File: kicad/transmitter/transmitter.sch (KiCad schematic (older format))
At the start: 30 parts, among them J1 Conn_01x02, J2 Conn_01x04, J3 AudioJack3, J4 AudioJack3, SW1 SW_SPST, SW2 SW_SPST, U1 ATmega328P-PU, U2 NRF24L01_Breakout, U3 MH-M18, U4 MSGEQ7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

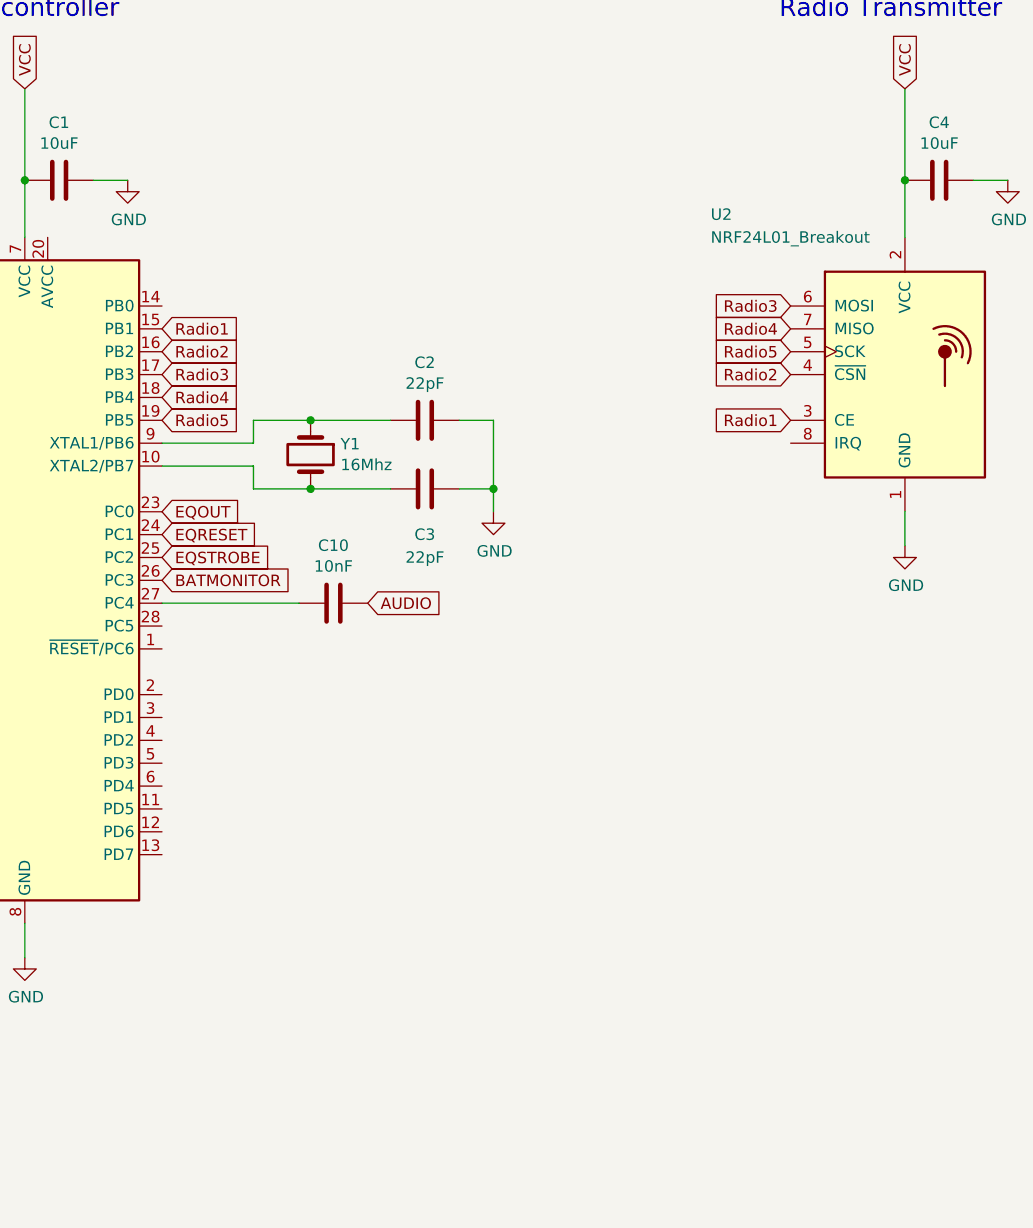
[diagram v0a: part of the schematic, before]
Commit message: Button, LEDs, ICSP header
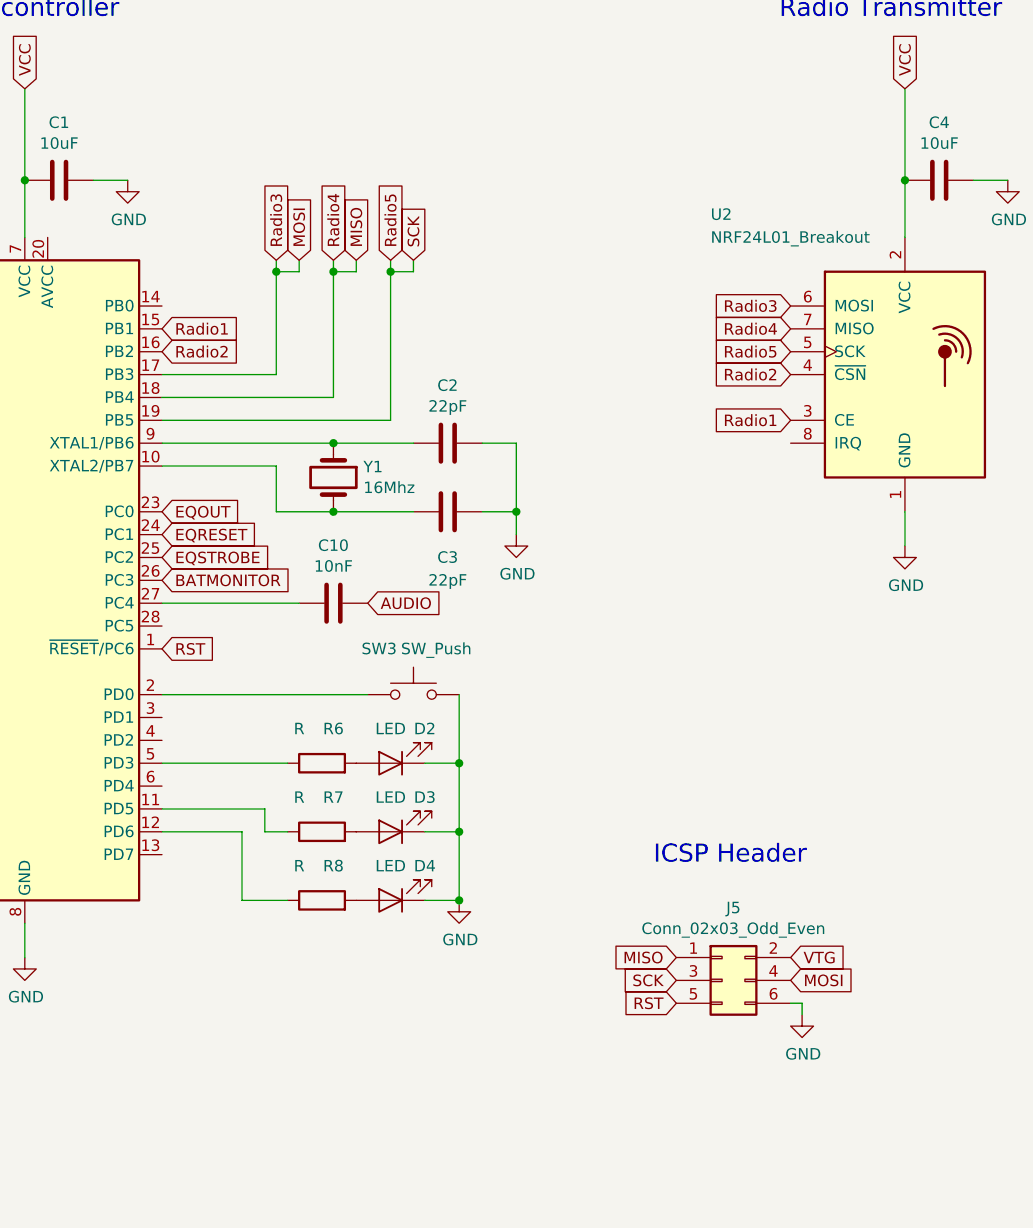
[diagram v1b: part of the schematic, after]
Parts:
- added D2, D3, D4: LED, LED_THT:LED_D3.0mm, symbol Device:LED
- added J5: Conn_02x03_Odd_Even, Connector_PinHeader_2.54mm:PinHeader_2x03_P2.54mm_Vertical, symbol Connector_Generic:Conn_02x03_Odd_Even
- added R6, R7, R8: R, Resistor_SMD:R_0603_1608Metric_Pad1.05x0.95mm_HandSolder, symbol Device:R
- added SW3: SW_Push, Connector_PinHeader_2.54mm:PinHeader_1x02_P2.54mm_Vertical, symbol Switch:SW_Push
- SW1, SW2: footprint Connector_Wire:SolderWirePad_1x02_P3.81mm_Drill1mm -> Connector_PinHeader_2.54mm:PinHeader_1x02_P2.54mm_Vertical
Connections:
- net GND: now also D2.1 (K), D3.1 (K), D4.1 (K), J5.6 (Pin_6), SW3.2
- net Radio5: now also J5.3 (Pin_3)
- net RST: now reaches U1.1 (~RESET~/PC6)
- net RST: now also J5.5 (Pin_5)
- net at U1.11 (PD5): now also R7.1
- net at U1.12 (PD6): now also R8.1
- net at U1.2 (PD0): now also SW3.1
- net at U1.5 (PD3): now also R6.1
- net Radio3 renamed MOSI
- net MOSI: now also J5.4 (Pin_4)
- net Radio4 renamed MISO
- net MISO: now also J5.1 (Pin_1)
- new net: D2.2 (A), R6.2
- new net: D3.2 (A), R7.2
- new net: D4.2 (A), R8.2
- new net VTG: J5.2 (Pin_2)
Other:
- note added: "ICSP Header"
- moved on the sheet: C2, C3, Y1

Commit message: Tidy-ups pre-order
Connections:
- no-connect marks 2 -> 9
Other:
- moved on the sheet: J5
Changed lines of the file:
@@
 L Connector_Generic:Conn_02x03_Odd_Even J5
 U 1 1 5E8614B4
-P 9250 5050
-F 0 "J5" H 9300 5367 50  0000 C CNN
-F 1 "Conn_02x03_Odd_Even" H 9300 5276 50  0000 C CNN
-F 2 "Connector_PinHeader_2.54mm:PinHeader_2x03_P2.54mm_Vertical" H 9250 5050 50  0001 C CNN
-F 3 "~" H 9250 5050 50  0001 C CNN
-	1    9250 5050
-	1    0    0    -1
-$EndComp
-Text GLabel 9050 4950 0    50   Input ~ 0
+P 9650 5350
+F 0 "J5" H 9700 5667 50  0000 C CNN
+F 1 "Conn_02x03_Odd_Even" H 9700 5576 50  0000 C CNN
+F 2 "Connector_PinHeader_2.54mm:PinHeader_2x03_P2.54mm_Vertical" H 9650 5350 50  0001 C CNN
+F 3 "~" H 9650 5350 50  0001 C CNN
+	1    9650 5350
+	1    0    0    -1
+$EndComp
+Text GLabel 9450 5250 0    50   Input ~ 0
 MISO
-Text GLabel 9550 4950 2    50   Input ~ 0
+Text GLabel 9950 5250 2    50   Input ~ 0
 VTG
-Text GLabel 9050 5050 0    50   Input ~ 0
+Text GLabel 9450 5350 0    50   Input ~ 0
 SCK
-Text GLabel 9550 5050 2    50   Input ~ 0
+Text GLabel 9950 5350 2    50   Input ~ 0
 MOSI
-Text GLabel 9050 5150 0    50   Input ~ 0
+Text GLabel 9450 5450 0    50   Input ~ 0
 RST
 $Comp
 L power:GND #PWR0118
 U 1 1 5E865C55
-P 9600 5200
-F 0 "#PWR0118" H 9600 4950 50  0001 C CNN
-F 1 "GND" H 9605 5027 50  0000 C CNN
-F 2 "" H 9600 5200 50  0001 C CNN
-F 3 "" H 9600 5200 50  0001 C CNN
-	1    9600 5200
-	1    0    0    -1
-$EndComp
-Wire Wire Line
-	9550 5150 9600 5150
-Wire Wire Line
-	9600 5150 9600 5200
-Text Notes 8950 4550 0    79   ~ 0
+P 10000 5500
+F 0 "#PWR0118" H 10000 5250 50  0001 C CNN
+F 1 "GND" H 10005 5327 50  0000 C CNN
+F 2 "" H 10000 5500 50  0001 C CNN
+F 3 "" H 10000 5500 50  0001 C CNN
+	1    10000 5500
+	1    0    0    -1
+$EndComp
+Wire Wire Line
+	9950 5450 10000 5450
+Wire Wire Line
+	10000 5450 10000 5500
+Text Notes 9350 4850 0    79   ~ 0
 ICSP Header
 Text GLabel 6800 3600 2    50   Input ~ 0
@@
 L power:GND #PWR0119
 U 1 1 5E43BBB8
-P 8100 4700
-F 0 "#PWR0119" H 8100 4450 50  0001 C CNN
-F 1 "GND" H 8105 4527 50  0000 C CNN
-F 2 "" H 8100 4700 50  0001 C CNN
-F 3 "" H 8100 4700 50  0001 C CNN
-	1    8100 4700
+P 8100 4950
+F 0 "#PWR0119" H 8100 4700 50  0001 C CNN
+F 1 "GND" H 8105 4777 50  0000 C CNN
+F 2 "" H 8100 4950 50  0001 C CNN
+F 3 "" H 8100 4950 50  0001 C CNN
+	1    8100 4950
 	1    0    0    -1
 $EndComp
@@
 Wire Wire Line
 	7950 4700 8100 4700
-Connection ~ 8100 4700
 Wire Wire Line
 	7950 4400 8100 4400
@@
 	8100 3800 8100 4100
 Connection ~ 8100 4100
+NoConn ~ 6800 3500
+NoConn ~ 6800 3900
+NoConn ~ 6800 4000
+NoConn ~ 6800 4200
+NoConn ~ 6800 4500
+NoConn ~ 6800 2100
+NoConn ~ 9550 2700
+Wire Wire Line
+	8100 4700 8100 4950
+Connection ~ 8100 4700
 $EndSCHEMATC

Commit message: Resistor and capacitor values
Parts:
- R3: value R -> 200k
- R4: value R -> 270k
- R5: value R -> 100k
- R6, R7, R8: value R -> 510
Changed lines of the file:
@@
 P 3800 6600
 F 0 "R3" V 3593 6600 50  0000 C CNN
-F 1 "R" V 3684 6600 50  0000 C CNN
+F 1 "200k" V 3684 6600 50  0000 C CNN
 F 2 "Resistor_SMD:R_0603_1608Metric_Pad1.05x0.95mm_HandSolder" V 3730 6600 50  0001 C CNN
 F 3 "~" H 3800 6600 50  0001 C CNN
@@
 P 3150 1550
 F 0 "R4" H 3080 1504 50  0000 R CNN
-F 1 "R" H 3080 1595 50  0000 R CNN
+F 1 "270k" H 3080 1595 50  0000 R CNN
 F 2 "Resistor_SMD:R_0603_1608Metric_Pad1.05x0.95mm_HandSolder" V 3080 1550 50  0001 C CNN
 F 3 "~" H 3150 1550 50  0001 C CNN
@@
 P 3150 1850
 F 0 "R5" H 3080 1804 50  0000 R CNN
-F 1 "R" H 3080 1895 50  0000 R CNN
+F 1 "100k" H 3080 1895 50  0000 R CNN
 F 2 "Resistor_SMD:R_0603_1608Metric_Pad1.05x0.95mm_HandSolder" V 3080 1850 50  0001 C CNN
 F 3 "~" H 3150 1850 50  0001 C CNN
@@
 P 7500 4100
 F 0 "R6" V 7650 4050 50  0000 C CNN
-F 1 "R" V 7650 4200 50  0000 C CNN
+F 1 "510" V 7650 4200 50  0000 C CNN
 F 2 "Resistor_SMD:R_0603_1608Metric_Pad1.05x0.95mm_HandSolder" V 7430 4100 50  0001 C CNN
 F 3 "~" H 7500 4100 50  0001 C CNN
@@
 P 7500 4400
 F 0 "R7" V 7650 4350 50  0000 C CNN
-F 1 "R" V 7650 4500 50  0000 C CNN
+F 1 "510" V 7650 4500 50  0000 C CNN
 F 2 "Resistor_SMD:R_0603_1608Metric_Pad1.05x0.95mm_HandSolder" V 7430 4400 50  0001 C CNN
 F 3 "~" H 7500 4400 50  0001 C CNN
@@
 P 7500 4700
 F 0 "R8" V 7650 4650 50  0000 C CNN
-F 1 "R" V 7650 4800 50  0000 C CNN
+F 1 "510" V 7650 4800 50  0000 C CNN
 F 2 "Resistor_SMD:R_0603_1608Metric_Pad1.05x0.95mm_HandSolder" V 7430 4700 50  0001 C CNN
 F 3 "~" H 7500 4700 50  0001 C CNN
